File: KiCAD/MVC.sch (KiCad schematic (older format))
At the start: 9 parts

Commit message: Working on basic schematic
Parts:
- removed U?: 6502, symbol 65XX:6502
- added C1, C2, C3, C4, C5, C6, C7, C8: 0.1uF, symbol Device:C
- added D1, D2, D3, D4: 1N4148, symbol Device:D
- added J2: Conn_02x02_Odd_Even, symbol Connector_Generic:Conn_02x02_Odd_Even
- added J3: Conn_01x22_Female, symbol Connector:Conn_01x22_Female
- added J?: Conn_02x23_Odd_Even, symbol Connector_Generic:Conn_02x23_Odd_Even
- added R1, R3: 1k, symbol Device:R
- added SW1: reset, symbol Switch:SW_Push
- added U5: 6522, symbol 65XX:6522
- added U6: 74HC00, symbol 74xx:74HC00
- added U7: 74LS30, symbol 74xx:74LS30
- added U?: 6502, symbol 65XX:6502
- U4: renamed from U?; symbol 65XX:62256 -> MVC-rescue:62256-65XX
- gave numbers to parts that had none: 4
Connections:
- net labels added: d0, d1, d2, d3, d4, d5, d6, d7, ~a13~, ~a14~
- wire segments 70 -> 251
- no-connect marks 0 -> 1
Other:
- moved on the sheet: J1, R2, U1A, U1B, U1C, U1E, U3

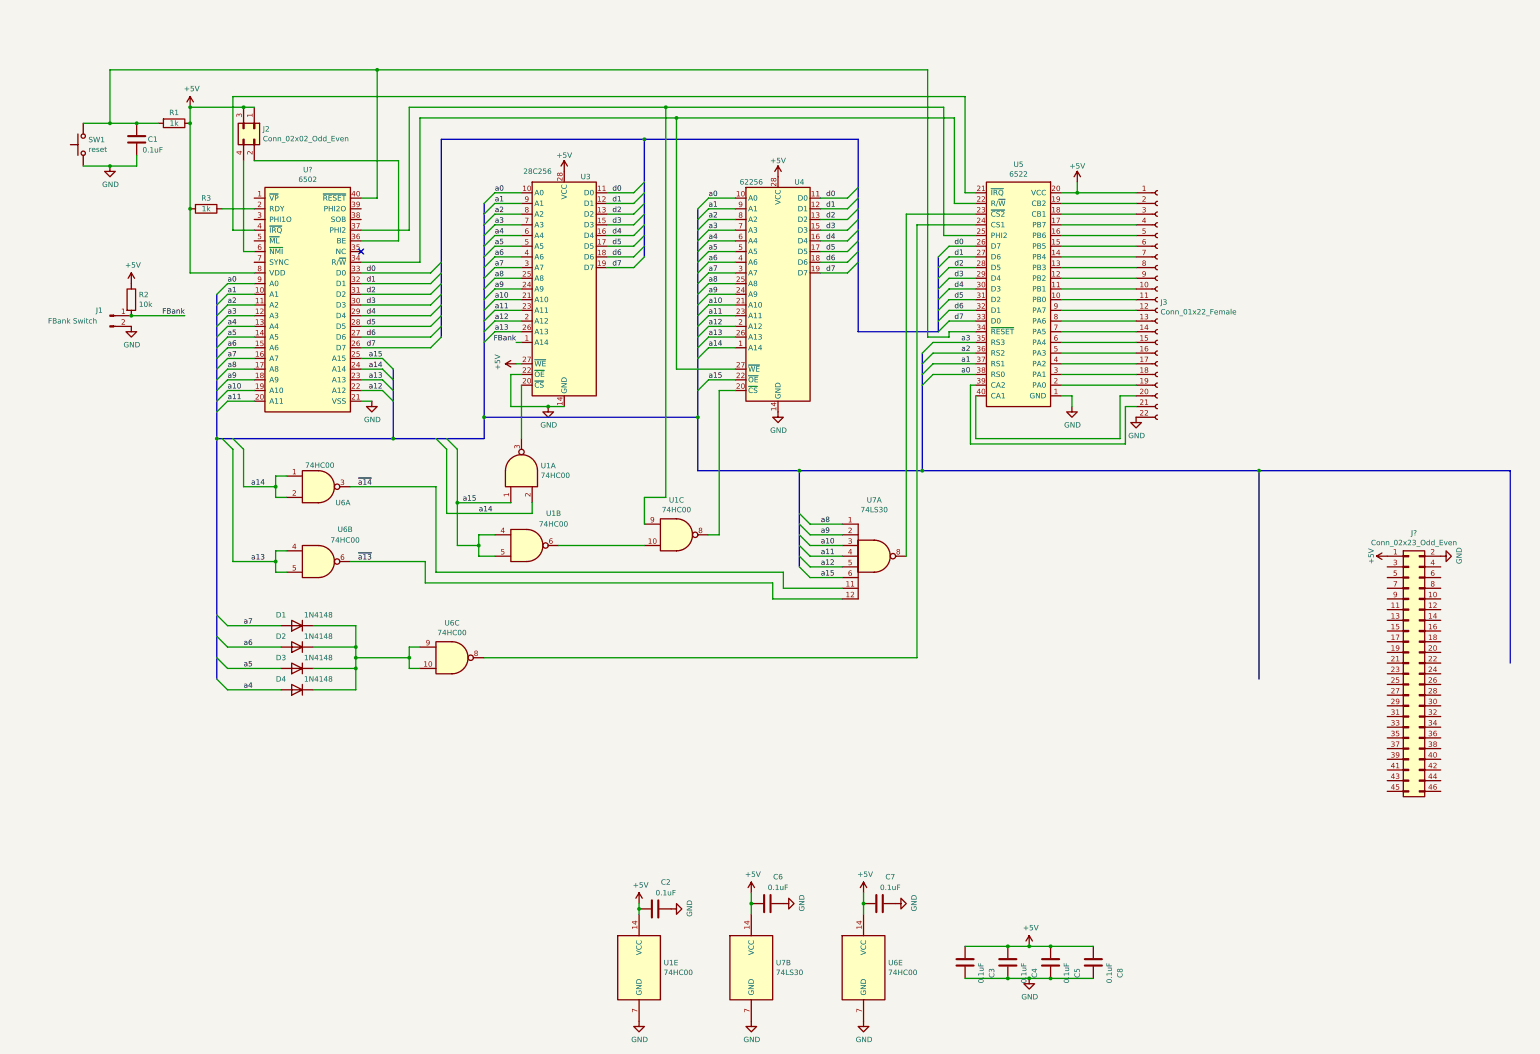
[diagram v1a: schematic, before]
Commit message: Finshed ugly schematic start on PCB
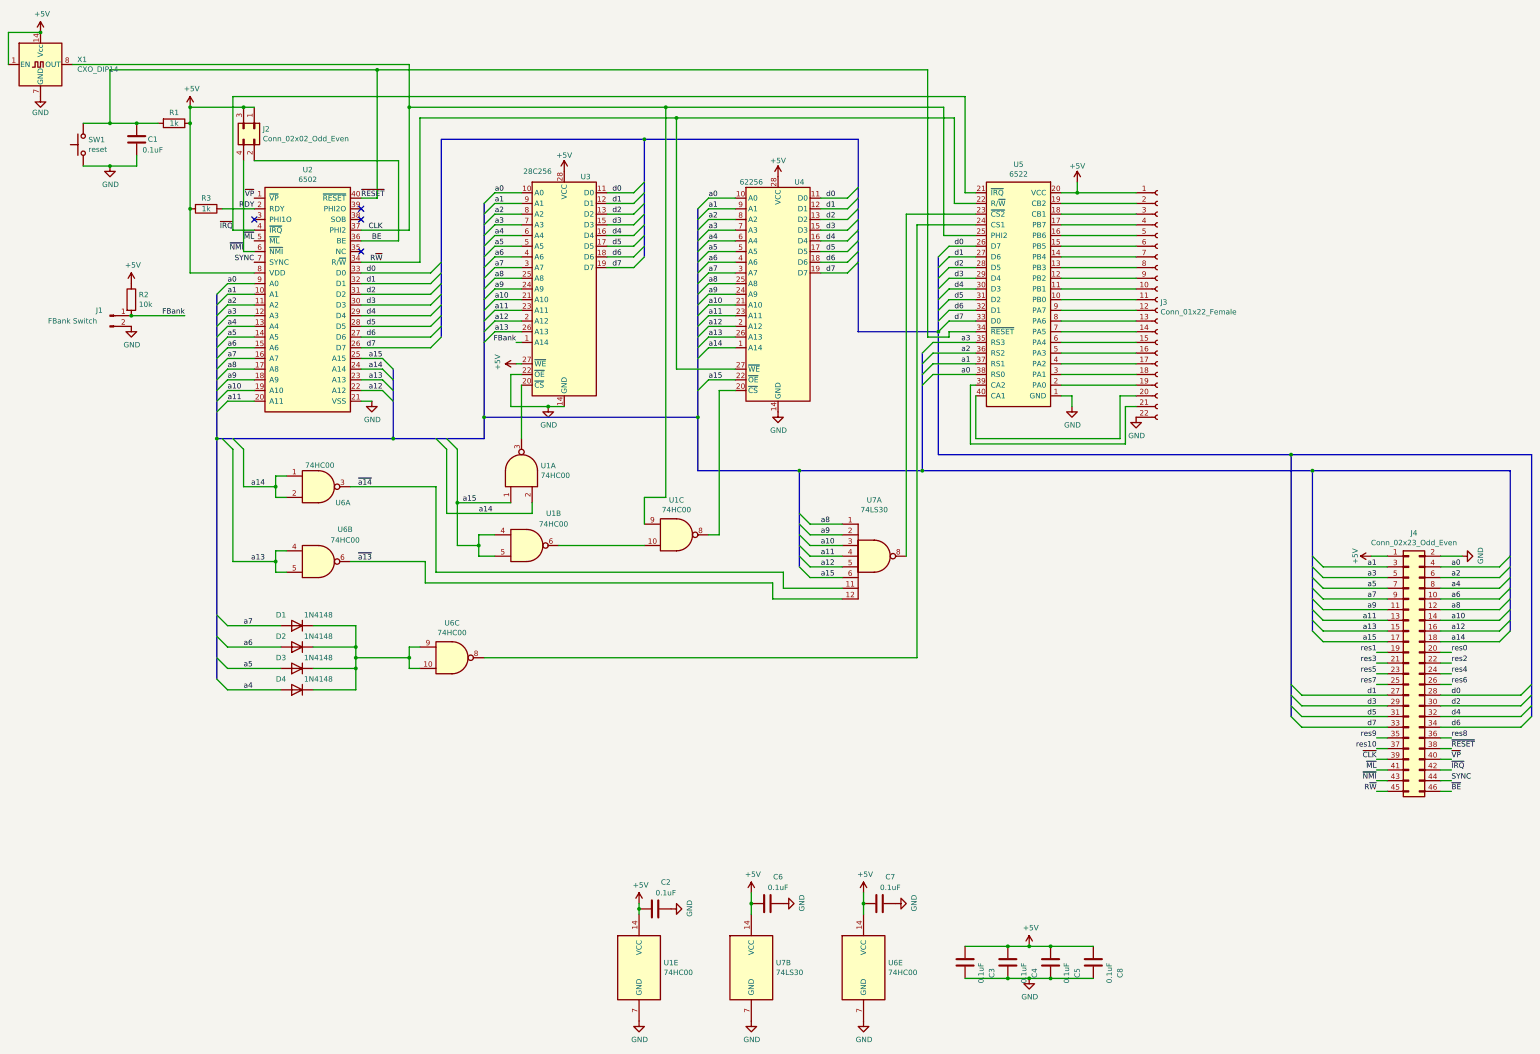
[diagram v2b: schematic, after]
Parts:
- added X1: CXO_DIP14, Oscillator:Oscillator_DIP-14, symbol Oscillator:CXO_DIP14
- C1, C2, C3, C4, C5, C6, C7, C8: footprint (none) -> Capacitor_THT:CP_Radial_D5.0mm_P2.50mm
- D1, D2, D3, D4: footprint (none) -> Diode_THT:D_A-405_P7.62mm_Horizontal
- J1: footprint (none) -> Connector_PinHeader_2.54mm:PinHeader_1x02_P2.54mm_Vertical
- J2: footprint (none) -> Connector_PinHeader_2.54mm:PinHeader_2x02_P2.54mm_Vertical
- J3: footprint (none) -> Connector_PinHeader_2.54mm:PinHeader_1x22_P2.54mm_Vertical
- J4: renamed from J?; footprint (none) -> Connector_PinHeader_2.54mm:PinHeader_2x23_P2.54mm_Vertical
- R1, R2, R3: footprint (none) -> Resistor_THT:R_Axial_DIN0207_L6.3mm_D2.5mm_P7.62mm_Horizontal
- SW1: footprint (none) -> Button_Switch_THT:SW_PUSH_6mm
- U1, U6, U7: footprint (none) -> Package_DIP:DIP-14_W7.62mm_Socket
- U2: renamed from U?; footprint (none) -> Package_DIP:DIP-40_W15.24mm_Socket
- U3, U4: footprint (none) -> Package_DIP:DIP-28_W15.24mm_Socket
- U5: footprint (none) -> Package_DIP:DIP-40_W15.24mm_Socket
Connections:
- net +5V: now also X1.1 (EN), X1.14 (Vcc)
- net GND: now also X1.7 (GND)
- net a0: now also J4.4 (Pin_4)
- net a1: now also J4.3 (Pin_3)
- net a10: now also J4.14 (Pin_14)
- net a11: now also J4.13 (Pin_13)
- net a12: now also J4.16 (Pin_16)
- net a13: now also J4.15 (Pin_15)
- net a14: now also J4.18 (Pin_18)
- net a15: now also J4.17 (Pin_17)
- net a2: now also J4.6 (Pin_6)
- net a3: now also J4.5 (Pin_5)
- net a4: now also J4.8 (Pin_8)
- net a5: now also J4.7 (Pin_7)
- net a6: now also J4.10 (Pin_10)
- net a7: now also J4.9 (Pin_9)
- net a8: now also J4.12 (Pin_12)
- net a9: now also J4.11 (Pin_11)
- net d0: now also J4.28 (Pin_28)
- net d1: now also J4.27 (Pin_27)
- net d2: now also J4.30 (Pin_30)
- net d3: now also J4.29 (Pin_29)
- net d4: now also J4.32 (Pin_32)
- net d5: now also J4.31 (Pin_31)
- net d6: now also J4.34 (Pin_34)
- net d7: now also J4.33 (Pin_33)
- net R~W~: now reaches U2.34 (R/~W~), U4.27 (~WE), U5.22 (R/~W~)
- net R~W~: now also J4.45 (Pin_45)
- net CLK: now reaches U1.9, U2.37 (PHI2), U5.25 (PHI2)
- net CLK: now also X1.8 (OUT)
- net RDY: now reaches R3.1, U2.2 (RDY)
- net ~RESET~: now reaches C1.1, R1.2, SW1.2, U2.40 (~RESET~), U5.34 (~RESET~)
- net ~RESET~: now also J4.38 (Pin_38)
- net BE: now reaches J2.2 (Pin_2), U2.36 (BE)
- net ~NMI~: now reaches J2.4 (Pin_4), U2.6 (~NMI~)
- net ~NMI~: now also J4.43 (Pin_43)
- net ~IRQ~: now reaches U2.4 (~IRQ~), U5.21 (~IRQ~)
- net ~IRQ~: now also J4.42 (Pin_42)
- net res1: now reaches J4.19 (Pin_19)
- net res0: now reaches J4.20 (Pin_20)
- net res3: now reaches J4.21 (Pin_21)
- net res2: now reaches J4.22 (Pin_22)
- net res5: now reaches J4.23 (Pin_23)
- net res4: now reaches J4.24 (Pin_24)
- net res7: now reaches J4.25 (Pin_25)
- net res6: now reaches J4.26 (Pin_26)
- net res9: now reaches J4.35 (Pin_35)
- net res8: now reaches J4.36 (Pin_36)
- net res10: now reaches J4.37 (Pin_37)
- net ~CLK~: now reaches J4.39 (Pin_39)
- net ~VP~: now reaches J4.40 (Pin_40)
- net ~VP~: now also U2.1 (~VP~)
- net ~ML~: now reaches J4.41 (Pin_41)
- net ~ML~: now also U2.5 (~ML~)
- net SYNC: now reaches J4.44 (Pin_44)
- net SYNC: now also U2.7 (SYNC)
- net ~BE~: now reaches J4.46 (Pin_46)
- no-connect marks 1 -> 4

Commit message: Built first ugly mainboard
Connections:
- net ~BE~ is gone; now on net BE: J4.46 (Pin_46)
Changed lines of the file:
@@
 CLK
 Text Label 14300 7850 0    50   ~ 0
-~BE~
+BE
 Text Label 13600 7850 2    50   ~ 0
 R~W~

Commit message: Fixed issues found in PCB over testing through apr
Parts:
- removed D1, D2, D3, D4: 1N4148, Diode_THT:D_A-405_P7.62mm_Horizontal, symbol Device:D
- added unit 4 of U6
- added U8: 74HC02, Package_DIP:DIP-14_W7.62mm_Socket, symbol 74xx:74HC02
- U2: symbol 65XX:6502 -> MVC-rescue:6502-65XX
- U5: symbol 65XX:6522 -> MVC-rescue:6522-65XX
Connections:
- net CLK is gone; now on net ~CLK~: U1.9, U2.37 (PHI2), U5.25 (PHI2), X1.8 (OUT)
- net a4: now also U8.6
- net a5: now also U8.5
- net a6: now also U8.3
- net a7: now also U8.2
- net d0: now also U5.33 (D0); no longer U5.26 (D7)
- net d1: now also U5.32 (D1); no longer U5.27 (D6)
- net d2: now also U5.31 (D2); no longer U5.28 (D5)
- net d3: now also U5.30 (D3); no longer U5.29 (D4)
- net d4: now also U5.29 (D4); no longer U5.30 (D3)
- net d5: now also U5.28 (D5); no longer U5.31 (D2)
- net d6: now also U5.27 (D6); no longer U5.32 (D1)
- net d7: now also U5.26 (D7); no longer U5.33 (D0)
- net at U6.10, U6.9: now also U6.11
- new net: U6.12, U8.1
- new net: U6.13, U8.4
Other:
- moved on the sheet: U6C
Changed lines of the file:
@@
 Connection ~ 3000 1450
 $Comp
-L 65XX:6522 U5
+L MVC-rescue:6522-65XX U5
 U 1 1 5F878B38
 P 10250 4250
@@
 	9850 2750 9600 2750
 Text Label 9650 2750 0    50   ~ 0
+d7
+Text Label 9650 2850 0    50   ~ 0
+d6
+Text Label 9650 2950 0    50   ~ 0
+d5
+Text Label 9650 3050 0    50   ~ 0
+d4
+Text Label 9650 3150 0    50   ~ 0
+d3
+Text Label 9650 3250 0    50   ~ 0
+d2
+Text Label 9650 3350 0    50   ~ 0
+d1
+Text Label 9650 3450 0    50   ~ 0
 d0
-Text Label 9650 2850 0    50   ~ 0
-d1
-Text Label 9650 2950 0    50   ~ 0
-d2
-Text Label 9650 3050 0    50   ~ 0
-d3
-Text Label 9650 3150 0    50   ~ 0
-d4
-Text Label 9650 3250 0    50   ~ 0
-d5
-Text Label 9650 3350 0    50   ~ 0
-d6
-Text Label 9650 3450 0    50   ~ 0
-d7
 $Comp
 L Device:C C8
@@
 L 74xx:74HC00 U6
 U 3 1 5FA976A2
-P 4950 6600
-F 0 "U6" H 4950 6925 50  0000 C CNN
-F 1 "74HC00" H 4950 6834 50  0000 C CNN
-F 2 "Package_DIP:DIP-14_W7.62mm_Socket" H 4950 6600 50  0001 C CNN
-F 3 "http://www.ti.com/lit/gpn/sn74hc00" H 4950 6600 50  0001 C CNN
-	3    4950 6600
-	1    0    0    -1
-$EndComp
-$Comp
-L Device:D D1
-U 1 1 5FA9BD48
-P 3500 6300
-F 0 "D1" H 3650 6200 50  0000 C CNN
-F 1 "1N4148" H 3300 6200 50  0000 C CNN
-F 2 "Diode_THT:D_A-405_P7.62mm_Horizontal" H 3500 6300 50  0001 C CNN
-F 3 "~" H 3500 6300 50  0001 C CNN
-	1    3500 6300
-	-1   0    0    1
-$EndComp
-$Comp
-L Device:D D2
-U 1 1 5FA9D040
-P 3500 6500
-F 0 "D2" H 3650 6400 50  0000 C CNN
-F 1 "1N4148" H 3300 6400 50  0000 C CNN
-F 2 "Diode_THT:D_A-405_P7.62mm_Horizontal" H 3500 6500 50  0001 C CNN
-F 3 "~" H 3500 6500 50  0001 C CNN
-	1    3500 6500
-	-1   0    0    1
-$EndComp
-$Comp
-L Device:D D3
-U 1 1 5FA9D35C
-P 3500 6700
-F 0 "D3" H 3650 6600 50  0000 C CNN
-F 1 "1N4148" H 3300 6600 50  0000 C CNN
-F 2 "Diode_THT:D_A-405_P7.62mm_Horizontal" H 3500 6700 50  0001 C CNN
-F 3 "~" H 3500 6700 50  0001 C CNN
-	1    3500 6700
-	-1   0    0    1
-$EndComp
-$Comp
-L Device:D D4
-U 1 1 5FA9D5B5
-P 3500 6900
-F 0 "D4" H 3650 6800 50  0000 C CNN
-F 1 "1N4148" H 3300 6800 50  0000 C CNN
-F 2 "Diode_THT:D_A-405_P7.62mm_Horizontal" H 3500 6900 50  0001 C CNN
-F 3 "~" H 3500 6900 50  0001 C CNN
-	1    3500 6900
-	-1   0    0    1
+P 5350 6600
+F 0 "U6" H 5350 6925 50  0000 C CNN
+F 1 "74HC00" H 5350 6834 50  0000 C CNN
+F 2 "Package_DIP:DIP-14_W7.62mm_Socket" H 5350 6600 50  0001 C CNN
+F 3 "http://www.ti.com/lit/gpn/sn74hc00" H 5350 6600 50  0001 C CNN
+	3    5350 6600
+	1    0    0    -1
 $EndComp
 Entry Wire Line
@@
 a4
 Wire Wire Line
-	3650 6300 4050 6300
-Wire Wire Line
-	4050 6300 4050 6500
-Wire Wire Line
-	3650 6500 4050 6500
-Connection ~ 4050 6500
-Wire Wire Line
-	4050 6500 4050 6600
-Wire Wire Line
-	3650 6900 4050 6900
-Wire Wire Line
-	3650 6700 4050 6700
-Connection ~ 4050 6700
-Wire Wire Line
-	4050 6700 4050 6900
-Wire Wire Line
-	4050 6600 4550 6600
-Wire Wire Line
-	4550 6600 4550 6500
-Wire Wire Line
-	4550 6500 4650 6500
-Connection ~ 4050 6600
-Wire Wire Line
-	4050 6600 4050 6700
-Wire Wire Line
-	4550 6600 4550 6700
-Wire Wire Line
-	4550 6700 4650 6700
-Connection ~ 4550 6600
+	4950 6500 5050 6500
+Wire Wire Line
+	4950 6700 5050 6700
 Wire Wire Line
 	9850 2550 9300 2550
@@
 	9300 2550 9300 6600
 Wire Wire Line
-	9300 6600 5250 6600
+	9300 6600 5650 6600
 Connection ~ 2750 4550
 Connection ~ 4400 4550
@@
 $EndComp
 $Comp
-L 65XX:6502 U2
+L MVC-rescue:6502-65XX U2
 U 1 1 5FFC5BE1
 P 3600 3200
@@
 	4550 1050 4550 1450
 Text Label 4300 2600 2    50   ~ 0
-CLK
+~CLK~
 Text Label 14300 7850 0    50   ~ 0
 BE
@@
 Wire Wire Line
 	14300 7350 14200 7350
+Wire Wire Line
+	4950 6500 4950 6600
+$Comp
+L 74xx:74HC00 U6
+U 4 1 609C19CC
+P 4650 6600
+F 0 "U6" H 4650 6925 50  0000 C CNN
+F 1 "74HC00" H 4650 6834 50  0000 C CNN
+F 2 "Package_DIP:DIP-14_W7.62mm_Socket" H 4650 6600 50  0001 C CNN
+F 3 "http://www.ti.com/lit/gpn/sn74hc00" H 4650 6600 50  0001 C CNN
+	4    4650 6600
+	1    0    0    -1
+$EndComp
+Connection ~ 4950 6600
+Wire Wire Line
+	4950 6600 4950 6700
+$Comp
+L 74xx:74HC02 U8
+U 1 1 60B6F349
+P 3650 6400
+F 0 "U8" H 3650 6725 50  0000 C CNN
+F 1 "74HC02" H 3650 6634 50  0000 C CNN
+F 2 "Package_DIP:DIP-14_W7.62mm_Socket" H 3650 6400 50  0001 C CNN
+F 3 "http://www.ti.com/lit/gpn/sn74hc02" H 3650 6400 50  0001 C CNN
+	1    3650 6400
+	1    0    0    -1
+$EndComp
+$Comp
+L 74xx:74HC02 U8
+U 2 1 60B70E88
+P 3650 6800
+F 0 "U8" H 3650 6500 50  0000 C CNN
+F 1 "74HC02" H 3650 6600 50  0000 C CNN
+F 2 "Package_DIP:DIP-14_W7.62mm_Socket" H 3650 6800 50  0001 C CNN
+F 3 "http://www.ti.com/lit/gpn/sn74hc02" H 3650 6800 50  0001 C CNN
+	2    3650 6800
+	1    0    0    -1
+$EndComp
+Wire Wire Line
+	3950 6400 3950 6500
+Wire Wire Line
+	3950 6500 4350 6500
+Wire Wire Line
+	3950 6800 3950 6700
+Wire Wire Line
+	3950 6700 4350 6700
 Wire Bus Line
 	4400 4550 5250 4550
